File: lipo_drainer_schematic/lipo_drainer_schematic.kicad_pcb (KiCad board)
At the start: 2 copper layers, 122 x 88 mm, 63 parts, among them J1 BATT, J2 FAN, J3 Vcal, J4 128x64_OLED, J5 Gcal, J6 Ical, J7 MCP7901, Q1 MMBT3904, Q10 G700P06T, Q11 G700P06T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

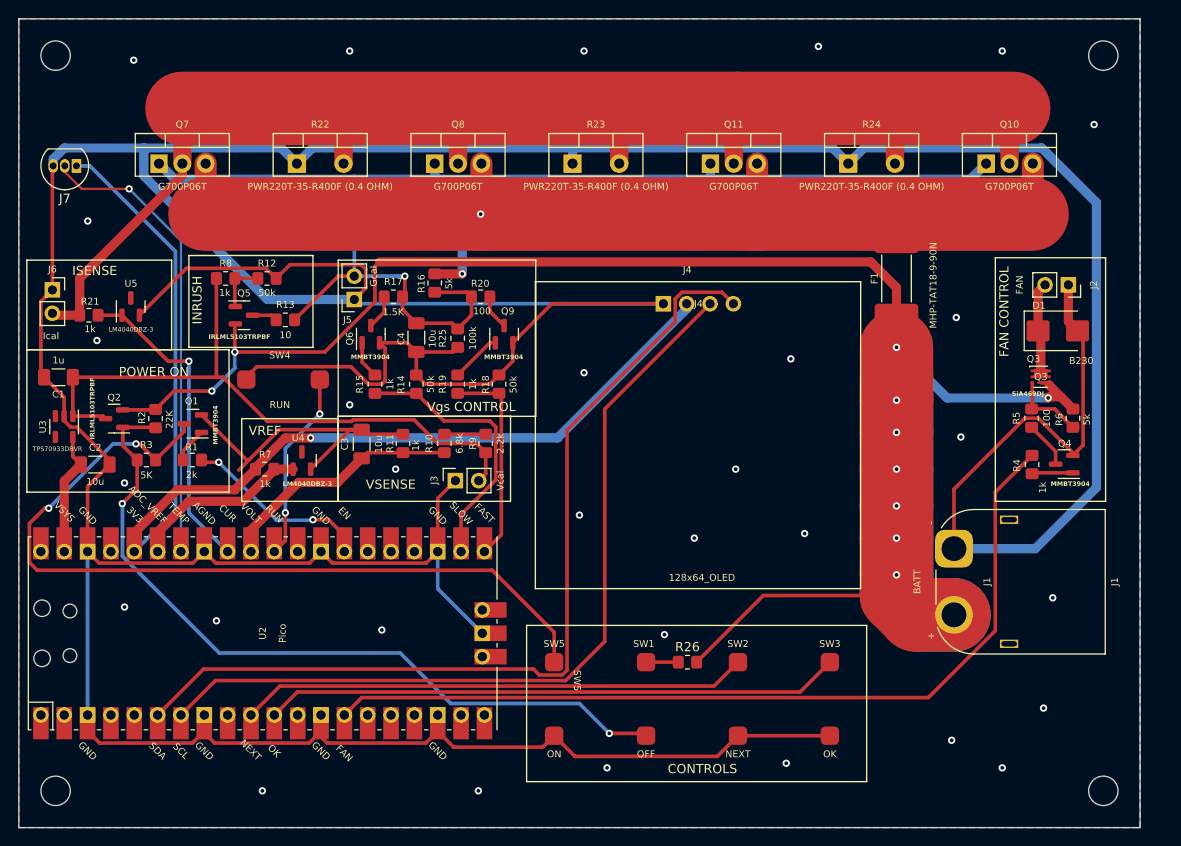
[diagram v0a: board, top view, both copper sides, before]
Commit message: Added Zener inductance protection.
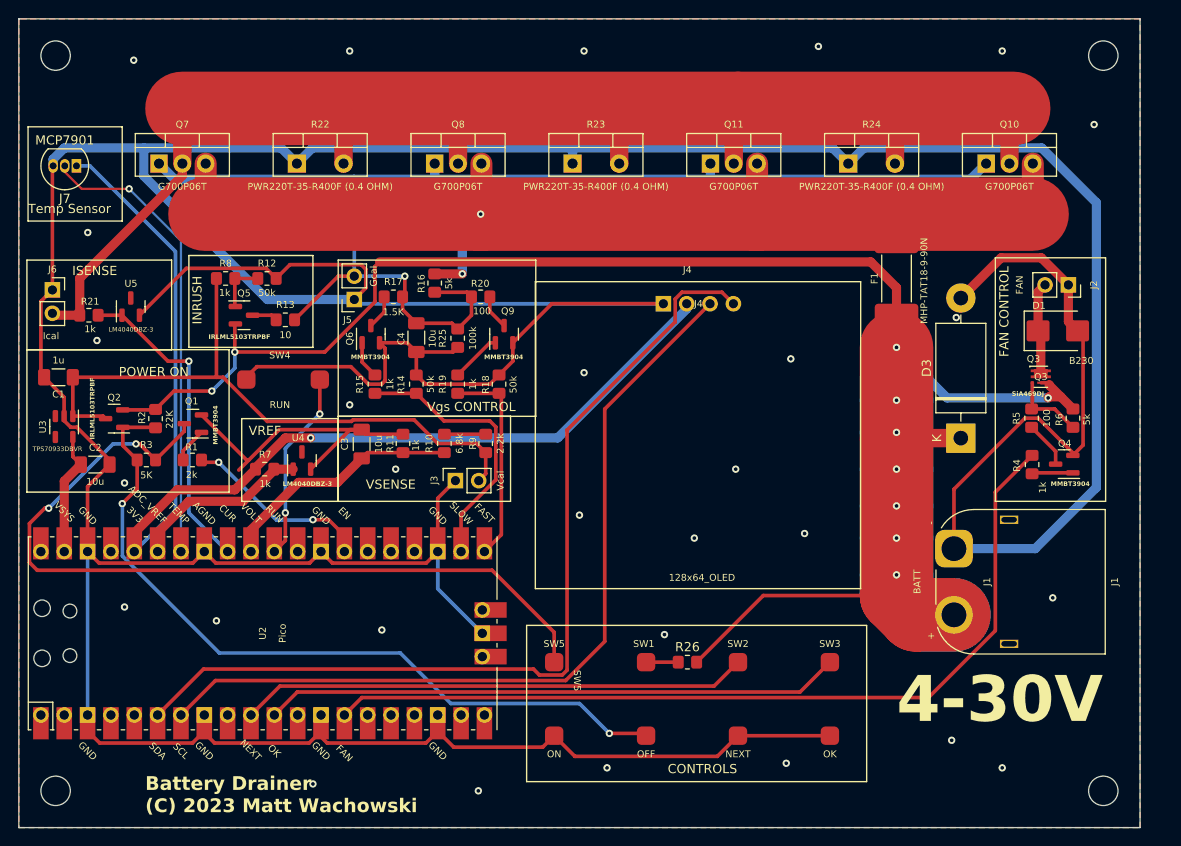
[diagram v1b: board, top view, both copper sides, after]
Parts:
- added D3: 1N5363BG, Diode_THT:D_DO-201AD_P15.24mm_Horizontal, F.Cu at (190.5, 95.6)
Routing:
- net GND: track 635.0 -> 649.8 mm, vias 31 -> 30
- net /BAT+: track 216.1 -> 223.2 mm
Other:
- board text added: "4-30V"
- board text added: "Battery Drainer (C) 2023 Matt Wachowski"
- board text added: "Temp Sensor"

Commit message: Enlarge power vias, update schematic
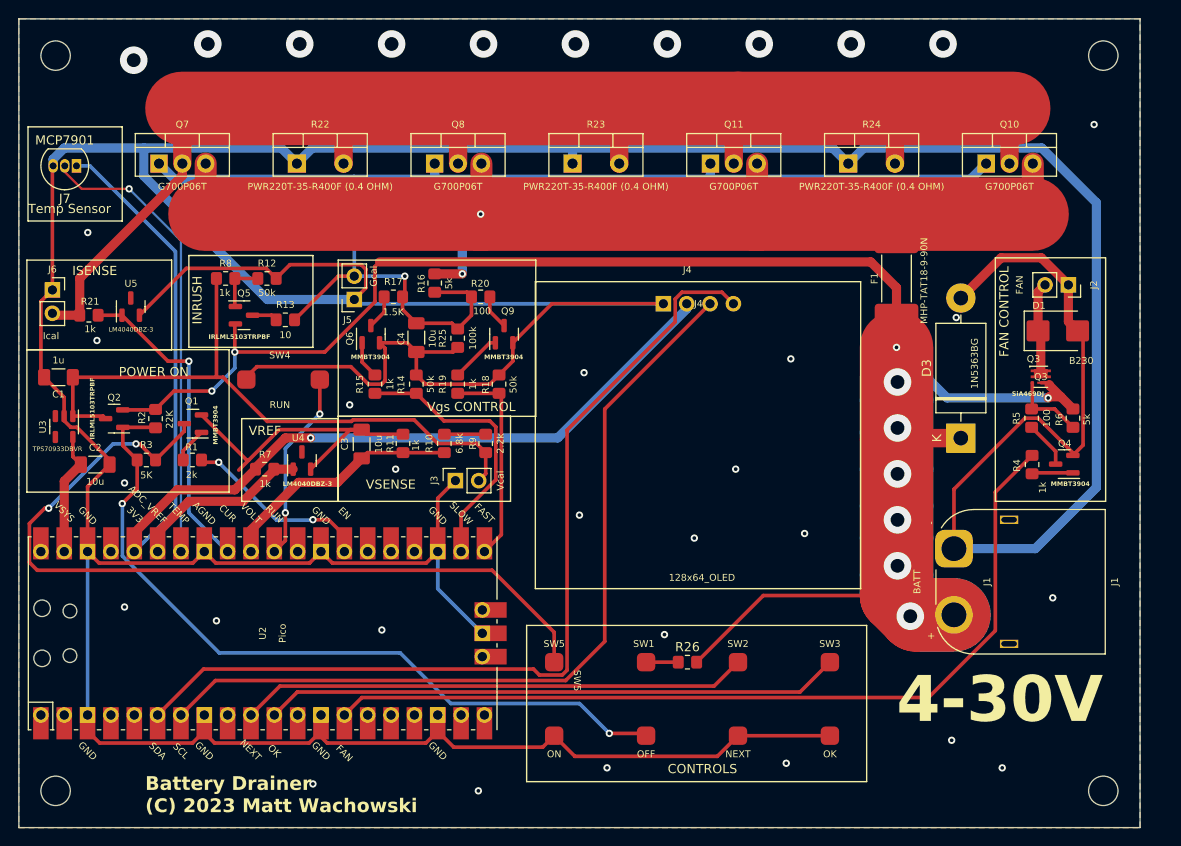
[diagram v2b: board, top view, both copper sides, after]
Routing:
- net GND: vias 30 -> 35
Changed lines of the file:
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@@
         (effects (font (size 1 1) (thickness 0.15)))
     )
-    (fp_text value "1N5363BG" (at 7.62 3.72 90) (layer "F.Fab")
-        (effects (font (size 1 1) (thickness 0.15)))
+    (fp_text value "1N5363BG" (at 8.12 1.5 90) (layer "F.SilkS")
+        (effects (font (size 0.75 0.75) (thickness 0.15)))
     )
     (fp_text user "K" (at 0 -2.6 90) (layer "F.SilkS")
@@
   (segment (start 111.5 86.25) (end 121.29 86.25) (width 0.4) (layer "F.Cu") (net 9))
   (segment (start 202.7 92.45) (end 201.375 91.125) (width 1) (layer "F.Cu") (net 9))
+  (via (at 183.606867 109.514738) (size 3) (drill 1.5) (layers "F.Cu" "B.Cu") (net 9))
   (via (at 200 91.25) (size 0.8) (drill 0.4) (layers "F.Cu" "B.Cu") (net 9))
-  (via (at 183.5 99) (size 0.8) (drill 0.4) (layers "F.Cu" "B.Cu") (net 9))
-  (via (at 183.5 106.5) (size 0.8) (drill 0.4) (layers "F.Cu" "B.Cu") (net 9))
   (via (at 183.5 85.75) (size 0.8) (drill 0.4) (layers "F.Cu" "B.Cu") (net 9))
-  (via (at 183.5 91.5) (size 0.8) (drill 0.4) (layers "F.Cu" "B.Cu") (net 9))
-  (via (at 183.5 95) (size 0.8) (drill 0.4) (layers "F.Cu" "B.Cu") (net 9))
-  (via (at 183.5 103) (size 0.8) (drill 0.4) (layers "F.Cu" "B.Cu") (net 9))
-  (via (at 183.5 110.5) (size 0.8) (drill 0.4) (layers "F.Cu" "B.Cu") (net 9))
+  (via (at 185 115) (size 3) (drill 1.5) (layers "F.Cu" "B.Cu") (net 9))
+  (via (at 183.606867 94.514738) (size 3) (drill 1.5) (layers "F.Cu" "B.Cu") (net 9))
+  (via (at 183.606867 89.514738) (size 3) (drill 1.5) (layers "F.Cu" "B.Cu") (net 9))
+  (via (at 183.606867 99.514738) (size 3) (drill 1.5) (layers "F.Cu" "B.Cu") (net 9))
   (via (at 109 90.5) (size 0.8) (drill 0.4) (layers "F.Cu" "B.Cu") (net 9))
   (via (at 111.5 86.25) (size 0.8) (drill 0.4) (layers "F.Cu" "B.Cu") (net 9))
+  (via (at 183.606867 104.514738) (size 3) (drill 1.5) (layers "F.Cu" "B.Cu") (net 9))
   (segment (start 183.5 103) (end 183.5 99) (width 8) (layer "B.Cu") (net 9))
   (segment (start 183.5 91.5) (end 183.5 89) (width 8) (layer "B.Cu") (net 9))
@@
   (via (at 120 133.25) (size 0.8) (drill 0.4) (layers "F.Cu" "B.Cu") (free) (net 18))
   (via (at 172 87) (size 0.8) (drill 0.4) (layers "F.Cu" "B.Cu") (free) (net 18))
+  (via (at 108.56198 52.73477) (size 3) (drill 1.5) (layers "F.Cu" "B.Cu") (free) (net 18))
   (via (at 127.5 116.5) (size 0.8) (drill 0.4) (layers "F.Cu" "B.Cu") (free) (net 18))
+  (via (at 148.56198 52.73477) (size 3) (drill 1.5) (layers "F.Cu" "B.Cu") (free) (net 18))
   (via (at 96.5 85) (size 0.8) (drill 0.4) (layers "F.Cu" "B.Cu") (free) (net 18))
+  (via (at 118.56198 52.73477) (size 3) (drill 1.5) (layers "F.Cu" "B.Cu") (free) (net 18))
   (via (at 199.5 125) (size 0.8) (drill 0.4) (layers "F.Cu" "B.Cu") (free) (net 18))
   (via (at 152 131.5) (size 0.8) (drill 0.4) (layers "F.Cu" "B.Cu") (free) (net 18))
-  (via (at 124 53.5) (size 0.8) (drill 0.4) (layers "F.Cu" "B.Cu") (free) (net 18))
   (via (at 109.5 115.5) (size 0.8) (drill 0.4) (layers "F.Cu" "B.Cu") (free) (net 18))
   (via (at 161.5 106.5) (size 0.8) (drill 0.4) (layers "F.Cu" "B.Cu") (free) (net 18))
-  (via (at 100.5 54.5) (size 0.8) (drill 0.4) (layers "F.Cu" "B.Cu") (free) (net 18))
-  (via (at 195 53.5) (size 0.8) (drill 0.4) (layers "F.Cu" "B.Cu") (free) (net 18))
+  (via (at 100.5 54.5) (size 3) (drill 1.5) (layers "F.Cu" "B.Cu") (free) (net 18))
   (via (at 171.5 131) (size 0.8) (drill 0.4) (layers "F.Cu" "B.Cu") (free) (net 18))
+  (via (at 188.56198 52.73477) (size 3) (drill 1.5) (layers "F.Cu" "B.Cu") (free) (net 18))
   (via (at 129 99) (size 0.8) (drill 0.4) (layers "F.Cu" "B.Cu") (free) (net 18))
   (via (at 158.25 117) (size 0.8) (drill 0.4) (layers "F.Cu" "B.Cu") (free) (net 18))
-  (via (at 175 53) (size 0.8) (drill 0.4) (layers "F.Cu" "B.Cu") (free) (net 18))
   (via (at 200.5 113) (size 0.8) (drill 0.4) (layers "F.Cu" "B.Cu") (free) (net 18))
+  (via (at 168.56198 52.73477) (size 3) (drill 1.5) (layers "F.Cu" "B.Cu") (free) (net 18))
+  (via (at 128.56198 52.73477) (size 3) (drill 1.5) (layers "F.Cu" "B.Cu") (free) (net 18))
   (via (at 124 92) (size 0.8) (drill 0.4) (layers "F.Cu" "B.Cu") (free) (net 18))
   (via (at 99.5 114) (size 0.8) (drill 0.4) (layers "F.Cu" "B.Cu") (free) (net 18))
@@
   (via (at 189.5 128.5) (size 0.8) (drill 0.4) (layers "F.Cu" "B.Cu") (free) (net 18))
   (via (at 205 61.5) (size 0.8) (drill 0.4) (layers "F.Cu" "B.Cu") (free) (net 18))
+  (via (at 158.56198 52.73477) (size 3) (drill 1.5) (layers "F.Cu" "B.Cu") (free) (net 18))
   (via (at 95.5 73.25) (size 0.8) (drill 0.4) (layers "F.Cu" "B.Cu") (free) (net 18))
   (via (at 166 99) (size 0.8) (drill 0.4) (layers "F.Cu" "B.Cu") (free) (net 18))
   (via (at 149 104) (size 0.8) (drill 0.4) (layers "F.Cu" "B.Cu") (free) (net 18))
+  (via (at 178.56198 52.73477) (size 3) (drill 1.5) (layers "F.Cu" "B.Cu") (free) (net 18))
   (via (at 149.5 88.5) (size 0.8) (drill 0.4) (layers "F.Cu" "B.Cu") (free) (net 18))
   (via (at 138 134) (size 0.8) (drill 0.4) (layers "F.Cu" "B.Cu") (free) (net 18))
-  (via (at 149.5 53.5) (size 0.8) (drill 0.4) (layers "F.Cu" "B.Cu") (free) (net 18))
+  (via (at 138.56198 52.73477) (size 3) (drill 1.5) (layers "F.Cu" "B.Cu") (free) (net 18))
   (via (at 99.5 100.5) (size 0.8) (drill 0.4) (layers "F.Cu" "B.Cu") (free) (net 18))
   (via (at 173.5 106) (size 0.8) (drill 0.4) (layers "F.Cu" "B.Cu") (free) (net 18))

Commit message: Added motor BJT pulldown and redid ground planes
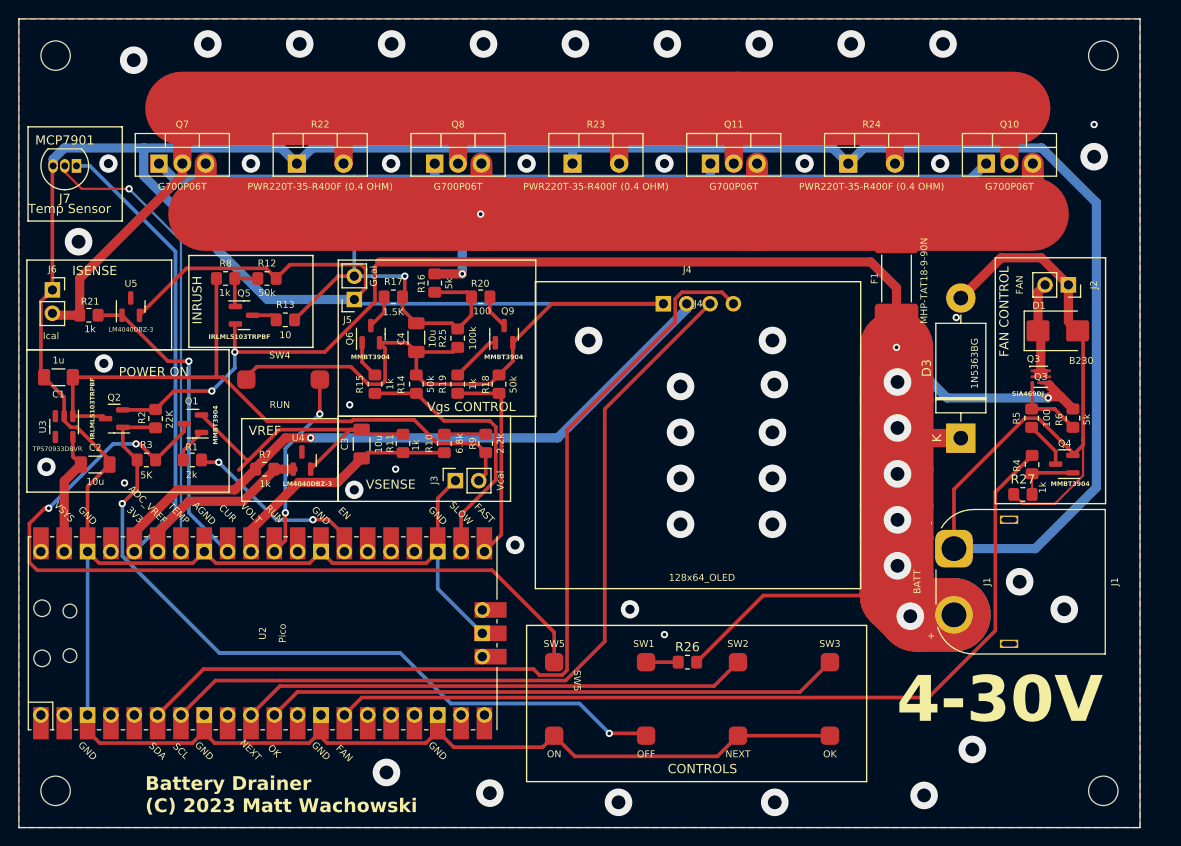
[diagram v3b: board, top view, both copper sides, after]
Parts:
- added R27: 50k, Resistor_SMD:R_0805_2012Metric_Pad1.20x1.40mm_HandSolder, F.Cu at (197.2, 101.8)
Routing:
- net GND: track 649.8 -> 663.0 mm, vias 35 -> 49
- net Net-(Q4-B): track 4.48 -> 6.73 mm

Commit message: Updated PCB layout
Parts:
- removed Q3: SiA469DJ, Package_TO_SOT_SMD:Vishay_PowerPAK_SC70-6L_Single
- removed Q4: MMBT3904, Package_TO_SOT_SMD:SOT-23
- removed R27: 50k, Resistor_SMD:R_0805_2012Metric_Pad1.20x1.40mm_HandSolder
- removed R4: 1k, Resistor_SMD:R_0805_2012Metric_Pad1.20x1.40mm_HandSolder
- removed R5: 100, Resistor_SMD:R_0805_2012Metric_Pad1.20x1.40mm_HandSolder
- removed R6: 5k, Resistor_SMD:R_0805_2012Metric_Pad1.20x1.40mm_HandSolder
- added C5: 10u, Capacitor_SMD:C_1206_3216Metric_Pad1.33x1.80mm_HandSolder, F.Cu at (148.0, 85.0)
- added C6: 1u, Capacitor_SMD:C_1206_3216Metric_Pad1.33x1.80mm_HandSolder, F.Cu at (149.6, 88.2)
- added J8: FAN2, Connector_PinSocket_2.54mm:PinSocket_1x04_P2.54mm_Vertical, F.Cu at (90.5, 74.2)
- added U1: MC7812BDTG, Package_TO_SOT_SMD:TO-252-2, F.Cu at (148.9, 96.5)
- F1: value MHP-TAT18-9-90N -> 40A Glass; footprint Fuse:Fuse_Schurter_UMZ250 -> Fuse:Fuseholder_Clip-6.3x32mm_Littelfuse_102_Inline_P34.21x7.62mm_D2.54mm_Horizontal
- J2: value FAN -> FAN1; footprint Connector_PinSocket_2.54mm:PinSocket_1x02_P2.54mm_Vertical -> Connector_PinSocket_2.54mm:PinSocket_1x04_P2.54mm_Vertical
- moved D1 52.0 mm to (149.2, 81.2)
- moved F1 33.4 mm to (202.5, 105.8)
- moved J2 14.8 mm to (187.4, 78.2), turned to 90 degrees
- moved R26 10.4 mm to (170.8, 117.2)
- moved J4 10.0 mm to (167.9, 83.2)
- moved J1 9.47 mm to (193.0, 116.5)
- moved SW1 9.25 mm to (165.5, 127.8)
- moved SW2 9.25 mm to (175.5, 119.8)
- moved SW3 9.25 mm to (185.5, 119.8)
- moved SW5 9.25 mm to (155.5, 119.8)
- moved D3 8.73 mm to (194.0, 103.6)
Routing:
- net /FAN+: track 10.1 -> 134.5 mm, vias 0 -> 1
- net GND: track 663.0 -> 551.4 mm, vias 49 -> 37
- net /FAN: track 95.4 -> 166.6 mm
- net /BAT+: track 223.2 -> 252.4 mm, vias 10 -> 6
- net /FET-S: track 122.5 -> 144.3 mm, vias 2 -> 3
- net /SCL: track 90.9 -> 105.2 mm
- net /OFF: track 84.0 -> 93.9 mm
- net /NEXT: track 55.4 -> 65.1 mm
- net /OK: track 62.8 -> 72.2 mm
- net /3V3: track 123.8 -> 133.0 mm
- net Net-(Q3-G): track 8.21 -> 0.00 mm
- net /ON: track 91.0 -> 98.3 mm
- net Net-(Q4-B): track 6.73 -> 0.00 mm
- net Net-(Q4-C): track 5.08 -> 0.00 mm
- net /SDA: track 99.5 -> 101.3 mm
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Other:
- board text added: "FAN_CTL"
- board text removed: "FAN CONTROL"
